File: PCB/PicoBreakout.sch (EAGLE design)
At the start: 40 parts

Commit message: updated run trace
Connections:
- new net N$64: JP1.20, X1.RUN
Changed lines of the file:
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@@
 <setting verticaltext="up"/>
 </settings>
-<grid distance="0.1" unitdist="inch" unit="inch" style="lines" multiple="1" display="no" altdistance="0.01" altunitdist="inch" altunit="inch"/>
+<grid distance="0.025" unitdist="inch" unit="inch" style="lines" multiple="1" display="no" altdistance="0.01" altunitdist="inch" altunit="inch"/>
 <layers>
 <layer number="1" name="Top" color="4" fill="1" visible="no" active="no"/>
@@
 </segment>
 </net>
+<net name="N$64" class="0">
+<segment>
+<pinref part="X1" gate="G$1" pin="RUN"/>
+<wire x1="106.68" y1="30.48" x2="113.03" y2="30.48" width="0.1524" layer="91"/>
+<wire x1="113.03" y1="30.48" x2="113.03" y2="34.29" width="0.1524" layer="91"/>
+<wire x1="113.03" y1="34.29" x2="150.495" y2="34.29" width="0.1524" layer="91"/>
+<wire x1="150.495" y1="34.29" x2="150.495" y2="17.78" width="0.1524" layer="91"/>
+<pinref part="JP1" gate="A" pin="20"/>
+<wire x1="150.495" y1="17.78" x2="144.78" y2="17.78" width="0.1524" layer="91"/>
+</segment>
+</net>

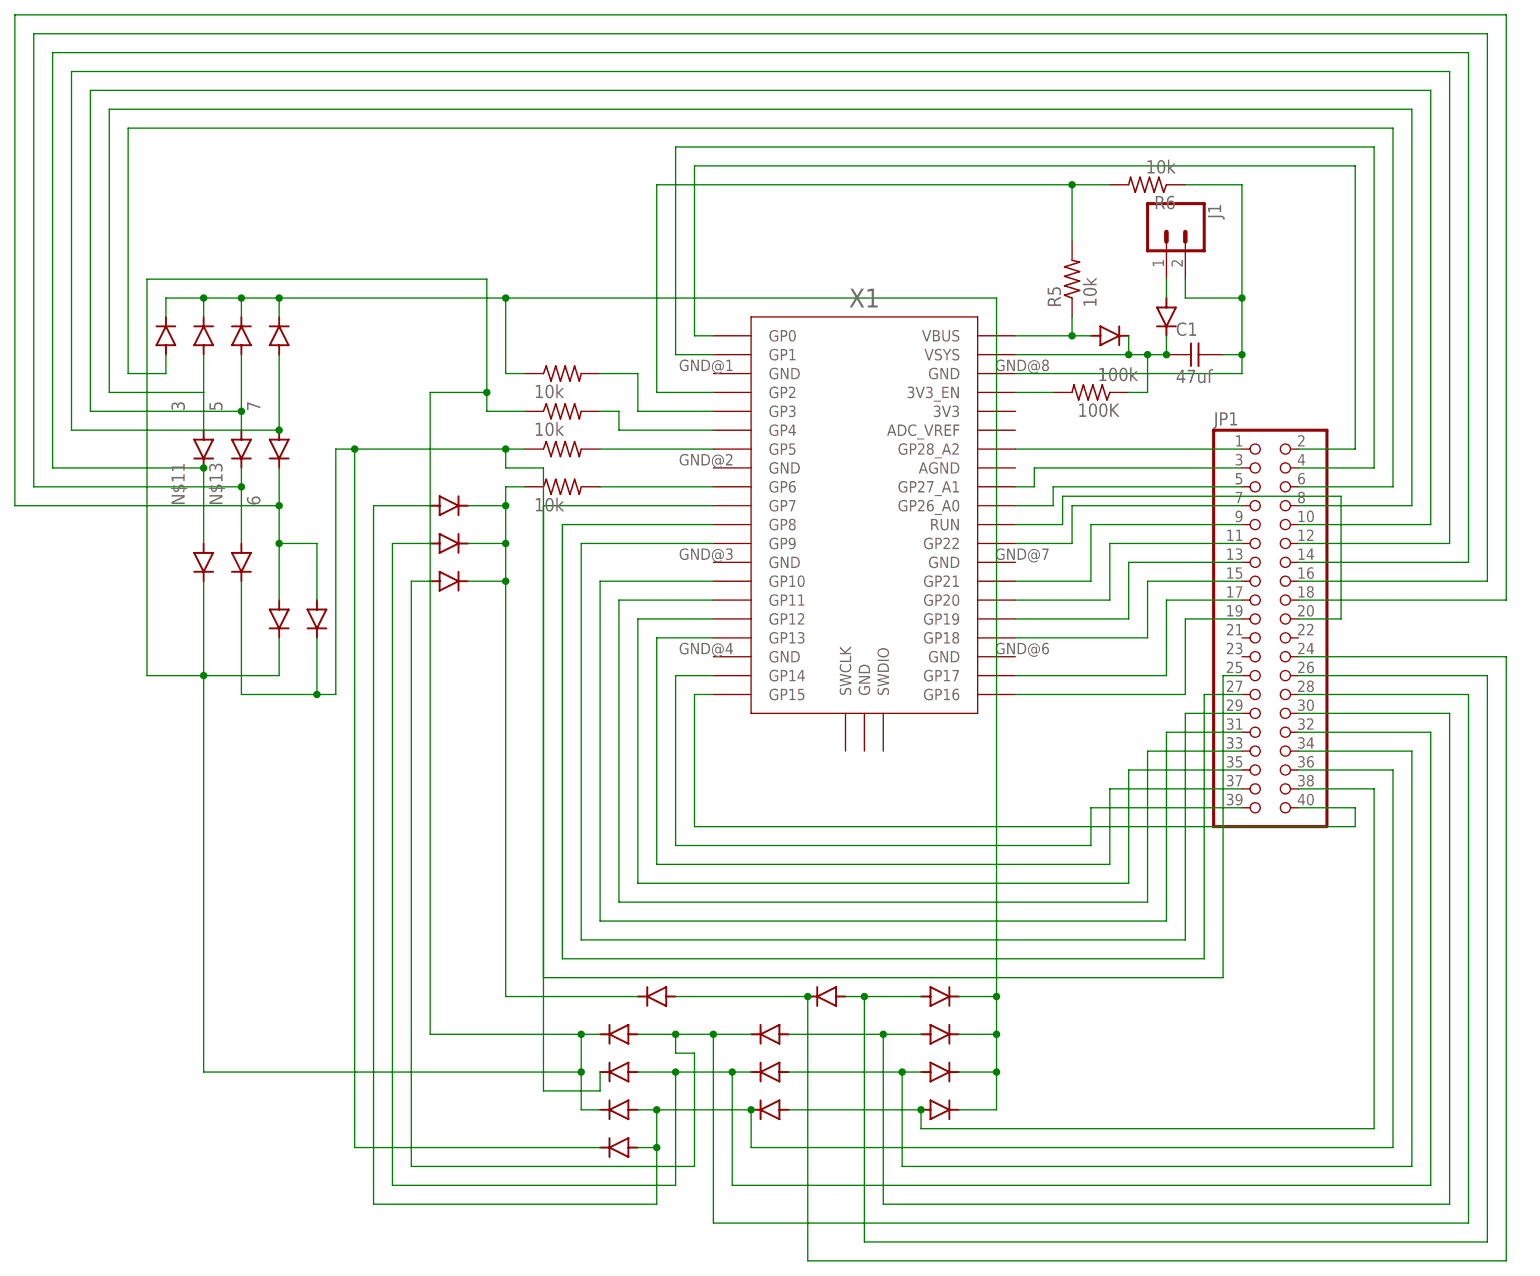
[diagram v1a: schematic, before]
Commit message: updated pico board
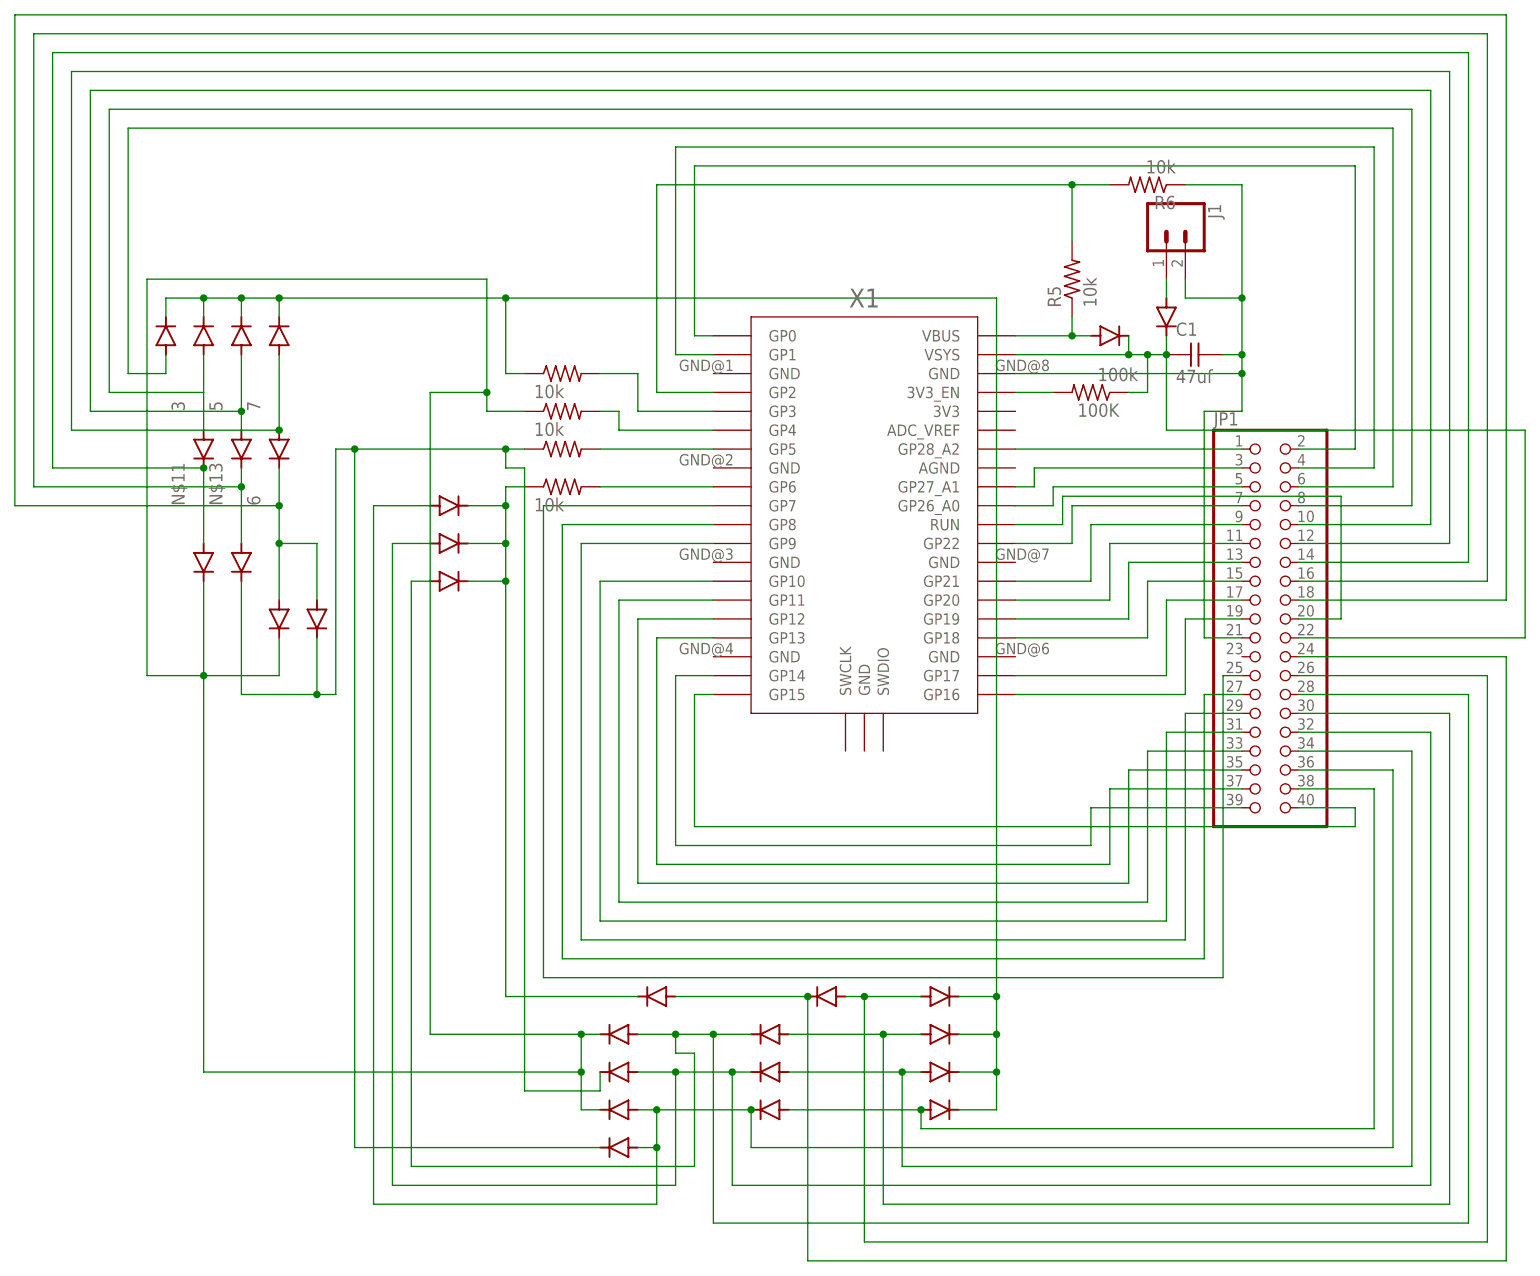
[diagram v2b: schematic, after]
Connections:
- net N$19: now also JP1.21
- net N$20: now also JP1.22
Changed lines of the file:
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@@
 <setting verticaltext="up"/>
 </settings>
-<grid distance="0.025" unitdist="inch" unit="inch" style="lines" multiple="1" display="no" altdistance="0.01" altunitdist="inch" altunit="inch"/>
+<grid distance="0.1" unitdist="inch" unit="inch" style="lines" multiple="1" display="no" altdistance="0.01" altunitdist="inch" altunit="inch"/>
 <layers>
 <layer number="1" name="Top" color="4" fill="1" visible="no" active="no"/>
@@
 <pinref part="D19" gate="G$1" pin="KATHODE"/>
 <wire x1="50.8" y1="-43.18" x2="50.8" y2="-45.72" width="0.1524" layer="91"/>
-<wire x1="50.8" y1="-45.72" x2="43.18" y2="-45.72" width="0.1524" layer="91"/>
-<wire x1="43.18" y1="-45.72" x2="43.18" y2="38.1" width="0.1524" layer="91"/>
-<wire x1="43.18" y1="38.1" x2="38.1" y2="38.1" width="0.1524" layer="91"/>
+<wire x1="50.8" y1="-45.72" x2="40.64" y2="-45.72" width="0.1524" layer="91"/>
+<wire x1="40.64" y1="-45.72" x2="40.64" y2="38.1" width="0.1524" layer="91"/>
+<wire x1="40.64" y1="38.1" x2="38.1" y2="38.1" width="0.1524" layer="91"/>
 <pinref part="R3" gate="G$1" pin="1"/>
 <wire x1="17.78" y1="40.64" x2="38.1" y2="40.64" width="0.1524" layer="91"/>
@@
 <junction x="137.16" y="60.96"/>
 <pinref part="X1" gate="G$1" pin="GND@8"/>
+<wire x1="137.16" y1="50.8" x2="137.16" y2="45.72" width="0.1524" layer="91"/>
+<wire x1="137.16" y1="45.72" x2="132.08" y2="45.72" width="0.1524" layer="91"/>
+<junction x="137.16" y="50.8"/>
+<pinref part="JP1" gate="A" pin="21"/>
+<wire x1="132.08" y1="45.72" x2="132.08" y2="15.24" width="0.1524" layer="91"/>
+<wire x1="132.08" y1="15.24" x2="137.16" y2="15.24" width="0.1524" layer="91"/>
 </segment>
 </net>
@@
 <junction x="124.46" y="53.34"/>
 <pinref part="X1" gate="G$1" pin="VSYS"/>
-</segment>
-</net>
+<wire x1="127" y1="53.34" x2="127" y2="43.18" width="0.1524" layer="91"/>
+<wire x1="127" y1="43.18" x2="175.26" y2="43.18" width="0.1524" layer="91"/>
+<wire x1="175.26" y1="43.18" x2="175.26" y2="15.24" width="0.1524" layer="91"/>
+<pinref part="JP1" gate="A" pin="22"/>
+<wire x1="175.26" y1="15.24" x2="144.78" y2="15.24" width="0.1524" layer="91"/>
+</segment>
+</net>
